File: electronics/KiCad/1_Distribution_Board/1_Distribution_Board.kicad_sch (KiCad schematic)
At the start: 9 parts, among them Q1 DMG2305UX, SW1 SW_Push

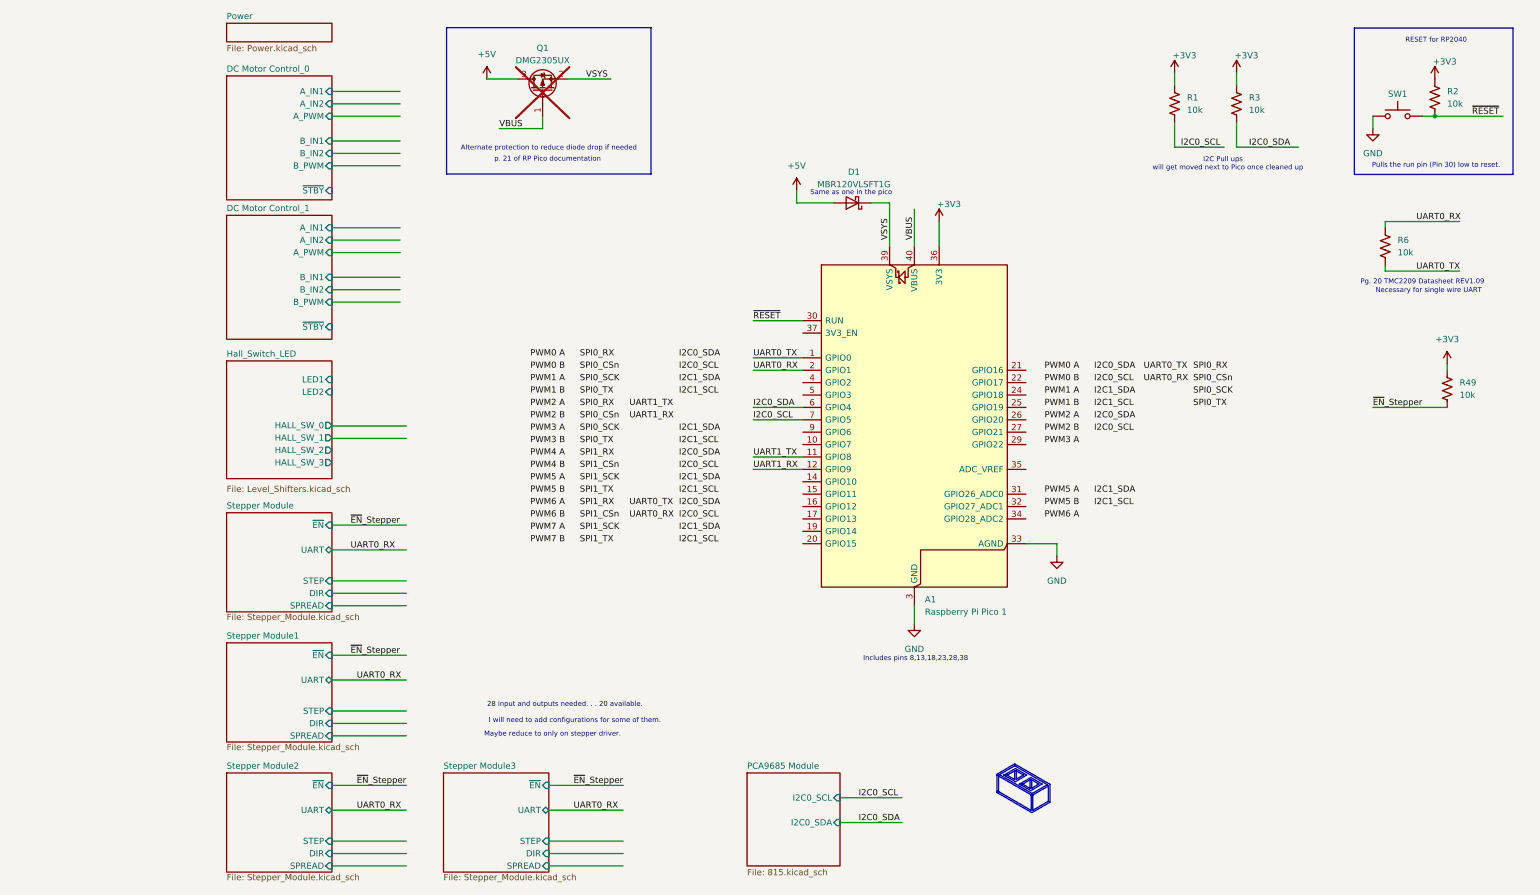
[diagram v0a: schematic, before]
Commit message: PCB updates
Added stepper module headers and working on silk for ease of debug.
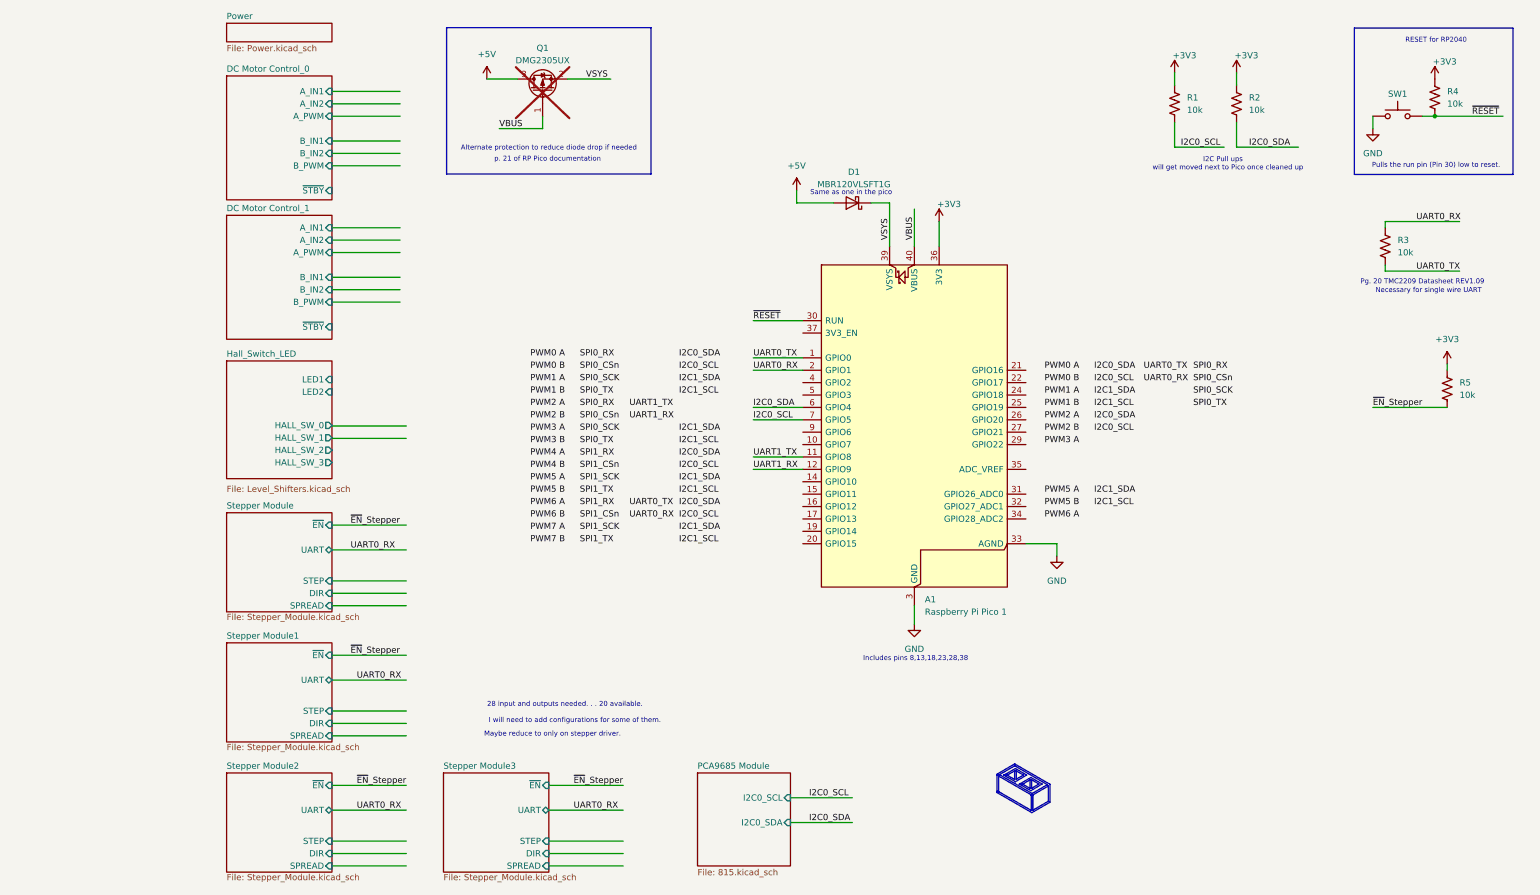
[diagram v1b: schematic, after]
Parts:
- renumbered R3 to R2, R6 to R3, R2 to R4, R49 to R5
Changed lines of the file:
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@@
 	(wire
 		(pts
-			(xy 146.05 173.99) (xy 158.75 173.99)
+			(xy 135.89 173.99) (xy 148.59 173.99)
 		)
 		(stroke
@@
 	(wire
 		(pts
-			(xy 146.05 179.07) (xy 158.75 179.07)
+			(xy 135.89 179.07) (xy 148.59 179.07)
 		)
 		(stroke
@@
 	)
 	(label "I2C0_SCL"
-		(at 149.86 173.99 0)
+		(at 139.7 173.99 0)
 		(effects
 			(font
@@
 	)
 	(label "I2C0_SDA"
-		(at 149.86 179.07 0)
+		(at 139.7 179.07 0)
 		(effects
 			(font
@@
 		(dnp no)
 		(fields_autoplaced yes)
-		(property "Reference" "#PWR0102"
+		(property "Reference" "#PWR010"
 			(at 270.51 88.9 0)
 			(effects
@@
 			(project "1_Distribution_Board"
 				(path "/d53c8c01-e754-4310-8a73-7d7c95e64cd3"
-					(reference "#PWR0102")
+					(reference "#PWR010")
 					(unit 1)
 				)
@@
 		(dnp no)
 		(fields_autoplaced yes)
-		(property "Reference" "#PWR06"
+		(property "Reference" "#PWR08"
 			(at 255.27 43.18 0)
 			(effects
@@
 			(project "1_Distribution_Board"
 				(path "/d53c8c01-e754-4310-8a73-7d7c95e64cd3"
-					(reference "#PWR06")
+					(reference "#PWR08")
 					(unit 1)
 				)
@@
 		(on_board yes)
 		(dnp no)
-		(property "Reference" "#PWR09"
+		(property "Reference" "#PWR07"
 			(at 227.33 29.21 0)
 			(effects
@@
 			(project "1_Distribution_Board"
 				(path "/d53c8c01-e754-4310-8a73-7d7c95e64cd3"
-					(reference "#PWR09")
+					(reference "#PWR07")
 					(unit 1)
 				)
@@
 		(dnp no)
 		(fields_autoplaced yes)
-		(property "Reference" "R6"
+		(property "Reference" "R3"
 			(at 260.35 59.6899 0)
 			(effects
@@
 			(project "1_Distribution_Board"
 				(path "/d53c8c01-e754-4310-8a73-7d7c95e64cd3"
-					(reference "R6")
+					(reference "R3")
 					(unit 1)
 				)
@@
 		(dnp no)
 		(fields_autoplaced yes)
-		(property "Reference" "R49"
+		(property "Reference" "R5"
 			(at 273.05 88.8999 0)
 			(effects
@@
 			(project "1_Distribution_Board"
 				(path "/d53c8c01-e754-4310-8a73-7d7c95e64cd3"
-					(reference "R49")
+					(reference "R5")
 					(unit 1)
 				)
@@
 		(on_board yes)
 		(dnp no)
-		(property "Reference" "#PWR08"
+		(property "Reference" "#PWR09"
 			(at 267.97 30.48 0)
 			(effects
@@
 			(project "1_Distribution_Board"
 				(path "/d53c8c01-e754-4310-8a73-7d7c95e64cd3"
-					(reference "#PWR08")
+					(reference "#PWR09")
 					(unit 1)
 				)
@@
 		(dnp no)
 		(fields_autoplaced yes)
-		(property "Reference" "R3"
+		(property "Reference" "R2"
 			(at 229.87 30.4799 0)
 			(effects
@@
 			(project "1_Distribution_Board"
 				(path "/d53c8c01-e754-4310-8a73-7d7c95e64cd3"
-					(reference "R3")
+					(reference "R2")
 					(unit 1)
 				)
@@
 		(on_board yes)
 		(dnp no)
-		(property "Reference" "#PWR07"
+		(property "Reference" "#PWR06"
 			(at 214.63 29.21 0)
 			(effects
@@
 			(project "1_Distribution_Board"
 				(path "/d53c8c01-e754-4310-8a73-7d7c95e64cd3"
-					(reference "#PWR07")
+					(reference "#PWR06")
 					(unit 1)
 				)
@@
 		(dnp no)
 		(fields_autoplaced yes)
-		(property "Reference" "R2"
+		(property "Reference" "R4"
 			(at 270.51 29.2099 0)
 			(effects
@@
 			(project ""
 				(path "/d53c8c01-e754-4310-8a73-7d7c95e64cd3"
-					(reference "R2")
+					(reference "R4")
 					(unit 1)
 				)
@@
 	)
 	(sheet
-		(at 127 168.91)
+		(at 116.84 168.91)
 		(size 19.05 19.05)
 		(exclude_from_sim no)
@@
 		)
 		(property "Sheetname" "PCA9685 Module"
-			(at 127 168.1984 0)
+			(at 116.84 168.1984 0)
 			(effects
 				(font
@@
 		)
 		(property "Sheetfile" "815.kicad_sch"
-			(at 127 188.5446 0)
+			(at 116.84 188.5446 0)
 			(effects
 				(font
@@
 		)
 		(pin "I2C0_SCL" input
-			(at 146.05 173.99 0)
+			(at 135.89 173.99 0)
 			(effects
 				(font
@@
 		)
 		(pin "I2C0_SDA" input
-			(at 146.05 179.07 0)
-			(effects
-				(font
+			(at 135.89 179.07 0)
+			(effects
+				(font

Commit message: Updated PCB/SCH
Updated stepper schematics and motor schematics for clarity. Updated motor module to use headers. Updated stepper driver top be the BIGTREETECH V1.3. Cleaned up layout locations a bit.
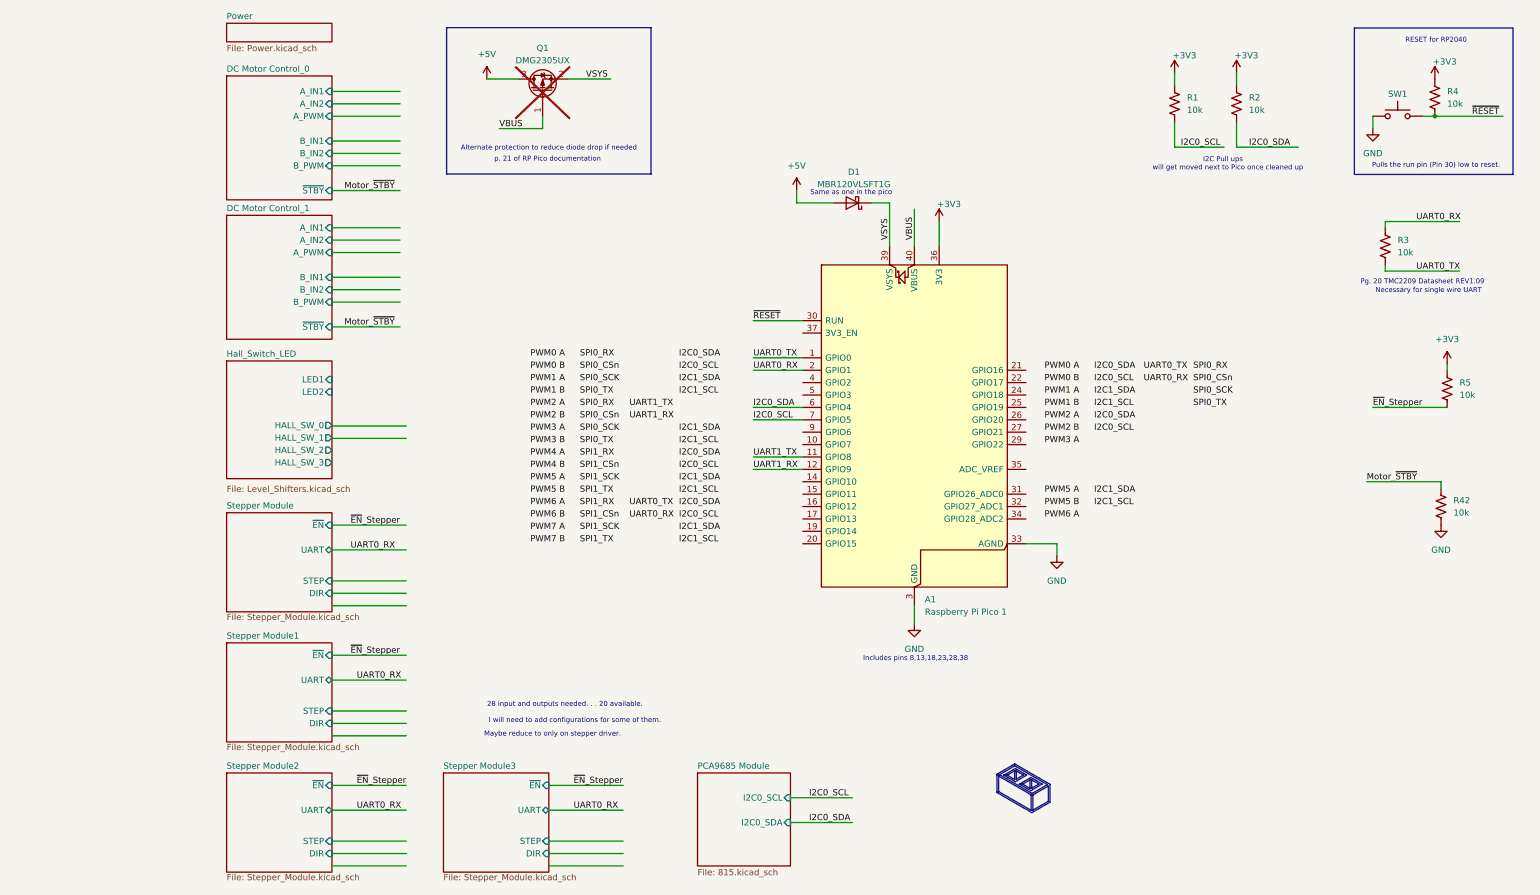
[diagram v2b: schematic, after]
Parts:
- added R42: 10k, Resistor_SMD:R_0805_2012Metric_Pad1.20x1.40mm_HandSolder, symbol Device:R_US
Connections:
- net GND: now also R42.2
- new net Motor_~{STBY}: R42.1
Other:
- sheet Stepper Module ports: added none; removed SPREAD
- sheet Stepper Module1 ports: added none; removed SPREAD
- sheet Stepper Module2 ports: added none; removed SPREAD
- sheet Stepper Module3 ports: added none; removed SPREAD
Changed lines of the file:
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@@
 	(wire
 		(pts
+			(xy 269.24 109.22) (xy 269.24 110.49)
+		)
+		(stroke
+			(width 0)
+			(type default)
+		)
+	)
+	(wire
+		(pts
 			(xy 86.36 171.45) (xy 101.6 171.45)
 		)
@@
 	(wire
 		(pts
+			(xy 41.91 49.53) (xy 55.88 49.53)
+		)
+		(stroke
+			(width 0)
+			(type default)
+		)
+	)
+	(wire
+		(pts
 			(xy 41.91 29.21) (xy 55.88 29.21)
 		)
@@
 	(wire
 		(pts
+			(xy 41.91 77.47) (xy 55.88 77.47)
+		)
+		(stroke
+			(width 0)
+			(type default)
+		)
+	)
+	(wire
+		(pts
 			(xy 135.89 173.99) (xy 148.59 173.99)
 		)
@@
 	(wire
 		(pts
+			(xy 254 109.22) (xy 269.24 109.22)
+		)
+		(stroke
+			(width 0)
+			(type default)
+		)
+	)
+	(wire
+		(pts
 			(xy 257.81 66.04) (xy 273.05 66.04)
 		)
@@
 		)
 	)
+	(label "Motor_~{STBY}"
+		(at 254 109.22 0)
+		(effects
+			(font
+				(size 1.27 1.27)
+			)
+			(justify left bottom)
+		)
+	)
 	(label "I2C1_SCL"
 		(at 113.03 91.44 0)
@@
 		)
 	)
+	(label "Motor_~{STBY}"
+		(at 44.45 49.53 0)
+		(effects
+			(font
+				(size 1.27 1.27)
+			)
+			(justify left bottom)
+		)
+	)
 	(label "SPI1_RX"
 		(at 92.71 104.14 0)
@@
 		)
 	)
+	(label "Motor_~{STBY}"
+		(at 44.45 77.47 0)
+		(effects
+			(font
+				(size 1.27 1.27)
+			)
+			(justify left bottom)
+		)
+	)
 	(label "I2C0_SDA"
 		(at 113.03 104.14 0)
@@
 	)
 	(symbol
+		(lib_id "power:GND")
+		(at 269.24 118.11 0)
+		(unit 1)
+		(exclude_from_sim no)
+		(in_bom yes)
+		(on_board yes)
+		(dnp no)
+		(fields_autoplaced yes)
+		(property "Reference" "#PWR033"
+			(at 269.24 124.46 0)
+			(effects
+				(font
+					(size 1.27 1.27)
+				)
+				(hide yes)
+			)
+		)
+		(property "Value" "GND"
+			(at 269.24 123.19 0)
+			(effects
+				(font
+					(size 1.27 1.27)
+				)
+			)
+		)
+		(property "Footprint" ""
+			(at 269.24 118.11 0)
+			(effects
+				(font
+					(size 1.27 1.27)
+				)
+				(hide yes)
+			)
+		)
+		(property "Datasheet" ""
+			(at 269.24 118.11 0)
+			(effects
+				(font
+					(size 1.27 1.27)
+				)
+				(hide yes)
+			)
+		)
+		(property "Description" "Power symbol creates a global label with name \"GND\" , ground"
+			(at 269.24 118.11 0)
+			(effects
+				(font
+					(size 1.27 1.27)
+				)
+				(hide yes)
+			)
+		)
+		(pin "1"
+		)
+		(instances
+			(project "1_Distribution_Board"
+				(path "/d53c8c01-e754-4310-8a73-7d7c95e64cd3"
+					(reference "#PWR033")
+					(unit 1)
+				)
+			)
+		)
+	)
+	(symbol
+		(lib_id "Device:R_US")
+		(at 269.24 114.3 0)
+		(unit 1)
+		(exclude_from_sim no)
+		(in_bom yes)
+		(on_board yes)
+		(dnp no)
+		(fields_autoplaced yes)
+		(property "Reference" "R42"
+			(at 271.78 113.0299 0)
+			(effects
+				(font
+					(size 1.27 1.27)
+				)
+				(justify left)
+			)
+		)
+		(property "Value" "10k"
+			(at 271.78 115.5699 0)
+			(effects
+				(font
+					(size 1.27 1.27)
+				)
+				(justify left)
+			)
+		)
+		(property "Footprint" "Resistor_SMD:R_0805_2012Metric_Pad1.20x1.40mm_HandSolder"
+			(at 270.256 114.554 90)
+			(effects
+				(font
+					(size 1.27 1.27)
+				)
+				(hide yes)
+			)
+		)
+		(property "Datasheet" "~"
+			(at 269.24 114.3 0)
+			(effects
+				(font
+					(size 1.27 1.27)
+				)
+				(hide yes)
+			)
+		)
+		(property "Description" "Resistor, US symbol"
+			(at 269.24 114.3 0)
+			(effects
+				(font
+					(size 1.27 1.27)
+				)
+				(hide yes)
+			)
+		)
+		(pin "2"
+		)
+		(pin "1"
+		)
+		(instances
+			(project "1_Distribution_Board"
+				(path "/d53c8c01-e754-4310-8a73-7d7c95e64cd3"
+					(reference "R42")
+					(unit 1)
+				)
+			)
+		)
+	)
+	(symbol
 		(lib_id "power:+3V3")
 		(at 227.33 25.4 0)
@@
 			)
 		)
-		(pin "SPREAD" input
-			(at 41.91 134.62 0)
-			(effects
-				(font
-					(size 1.27 1.27)
-				)
-				(justify right)
-			)
-		)
 		(pin "STEP" input
 			(at 41.91 129.54 0)
@@
 			)
 		)
-		(pin "SPREAD" input
-			(at 41.91 161.29 0)
-			(effects
-				(font
-					(size 1.27 1.27)
-				)
-				(justify right)
-			)
-		)
 		(pin "STEP" input
 			(at 41.91 156.21 0)
@@
 			)
 		)
-		(pin "SPREAD" input
-			(at 86.36 187.96 0)
-			(effects
-				(font
-					(size 1.27 1.27)
-				)
-				(justify right)
-			)
-		)
 		(pin "STEP" input
 			(at 86.36 182.88 0)
@@
 			(effects
 				(font
-					(size 1.27 1.27)
-				)
-				(justify right)
-			)
-		)
-		(pin "SPREAD" input
-			(at 41.91 187.96 0)
-			(effects
-				(font

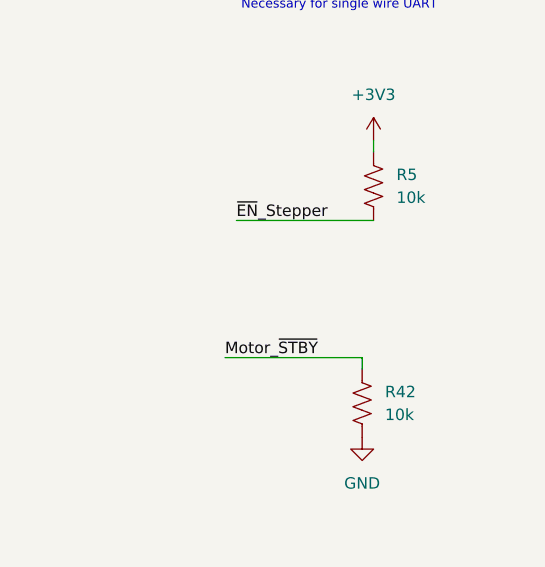
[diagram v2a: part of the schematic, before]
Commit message: Additional Routing and placement
Updated power page on schematic to remove redundant connections. Removed test points on steppers since the steppers drivers chosen have test points on them. Updated placement and cleaned up silk. Started placing final power connections.
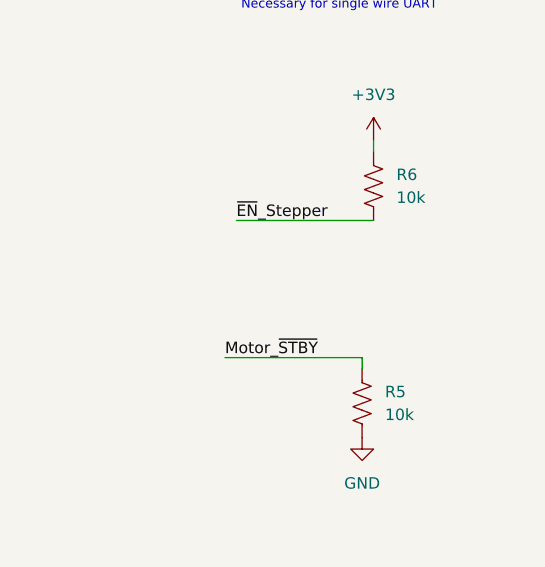
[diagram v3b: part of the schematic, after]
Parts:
- renumbered R42 to R5, R5 to R6
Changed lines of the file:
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@@
 		(dnp no)
 		(fields_autoplaced yes)
-		(property "Reference" "#PWR010"
+		(property "Reference" "#PWR011"
 			(at 270.51 88.9 0)
 			(effects
@@
 			(project "1_Distribution_Board"
 				(path "/d53c8c01-e754-4310-8a73-7d7c95e64cd3"
-					(reference "#PWR010")
+					(reference "#PWR011")
 					(unit 1)
 				)
@@
 		(dnp no)
 		(fields_autoplaced yes)
-		(property "Reference" "#PWR033"
+		(property "Reference" "#PWR010"
 			(at 269.24 124.46 0)
 			(effects
@@
 			(project "1_Distribution_Board"
 				(path "/d53c8c01-e754-4310-8a73-7d7c95e64cd3"
-					(reference "#PWR033")
+					(reference "#PWR010")
 					(unit 1)
 				)
@@
 		(dnp no)
 		(fields_autoplaced yes)
-		(property "Reference" "R42"
+		(property "Reference" "R5"
 			(at 271.78 113.0299 0)
 			(effects
@@
 			(project "1_Distribution_Board"
 				(path "/d53c8c01-e754-4310-8a73-7d7c95e64cd3"
-					(reference "R42")
+					(reference "R5")
 					(unit 1)
 				)
@@
 		(dnp no)
 		(fields_autoplaced yes)
-		(property "Reference" "R5"
+		(property "Reference" "R6"
 			(at 273.05 88.8999 0)
 			(effects
@@
 			(project "1_Distribution_Board"
 				(path "/d53c8c01-e754-4310-8a73-7d7c95e64cd3"
-					(reference "R5")
-					(unit 1)
-				)
+					(reference "R6")
+					(unit 1)
+				)
